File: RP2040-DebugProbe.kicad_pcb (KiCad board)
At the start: 2 copper layers, 55.9 x 25.4 mm, 60 parts, among them J1 CONN_MCU_JTAG, J10 CONN_USB, J2 CONN_MCU_UART, J3 CONN_DBG_COMB, J4 CONN_3V3_JUMPER, J7 CONN_DBG_JTAG, SW1 BOOTSEL, U1 W25Q128JVS, U2 RP2040, U3 74AUP1T17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

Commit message: Moved stuff around
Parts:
- moved D1 3.81 mm to (164.5, 104.1)
- moved D4 3.81 mm to (164.5, 99.0)
- moved D6 3.81 mm to (164.5, 111.7)
- moved D7 3.81 mm to (164.5, 116.8)
- moved J3 3.81 mm to (169.5, 99.1)
- moved J4 3.81 mm to (175.3, 99.0)
- moved J7 3.81 mm to (175.9, 118.1)
- moved R1 3.81 mm to (164.5, 105.4)
- moved R13 3.81 mm to (164.5, 115.6)
- moved R14 3.81 mm to (164.5, 102.9)
- moved R15 3.81 mm to (164.5, 100.3)
- moved R16 3.81 mm to (164.5, 114.3)
- moved R17 3.81 mm to (164.5, 113.0)
- moved R2 3.81 mm to (164.5, 97.8)
- moved R4 3.81 mm to (164.5, 110.5)
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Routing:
- net +3V3: track 44.1 -> 54.8 mm, vias 4 -> 7
- net XIN: track 0.00 -> 10.4 mm
- net MCU_RESET: track 0.00 -> 6.81 mm
- net XOUT: track 0.00 -> 5.68 mm
- net +1V1: track 10.3 -> 15.4 mm
- net SHIELD: track 7.66 -> 11.8 mm
- net VUSB: track 52.8 -> 49.0 mm
- net GND: track 2.28 -> 4.25 mm, vias 19 -> 21
- net USB_DN: track 21.5 -> 19.6 mm
- net USB_DP: track 21.6 -> 19.7 mm
- net QSPI_SD3: track 15.1 -> 13.2 mm
- net QSPI_SD1: track 12.3 -> 14.2 mm
- net QSPI_SD2: track 11.5 -> 13.4 mm
- net QSPI_SCLK: track 12.9 -> 11.1 mm
- net QSPI_SS: track 25.1 -> 26.9 mm
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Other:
- board size 55.9 x 25.4 mm -> 50.8 x 25.4 mm
- board text added: "G"
- board text added: "R"
- board text added: "T"

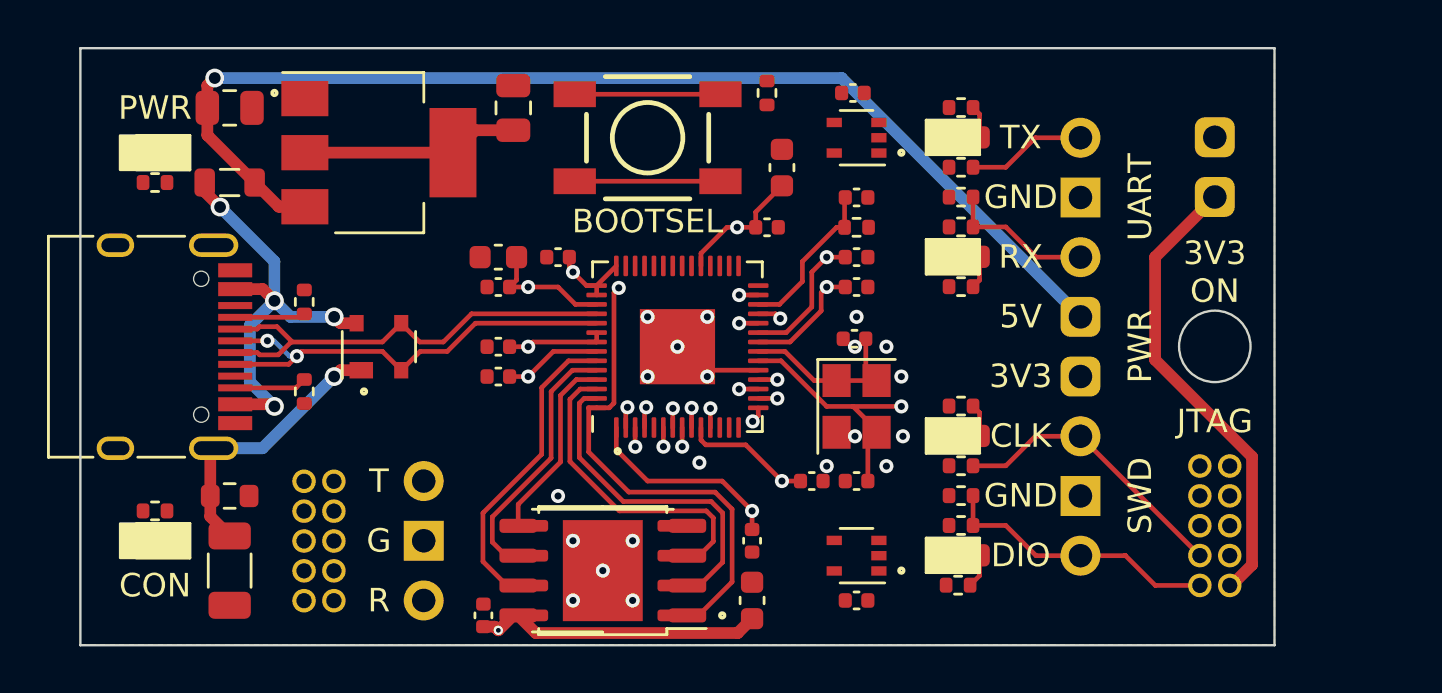
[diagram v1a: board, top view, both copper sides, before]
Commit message: Made the board 4 layer. Made a basic routing.
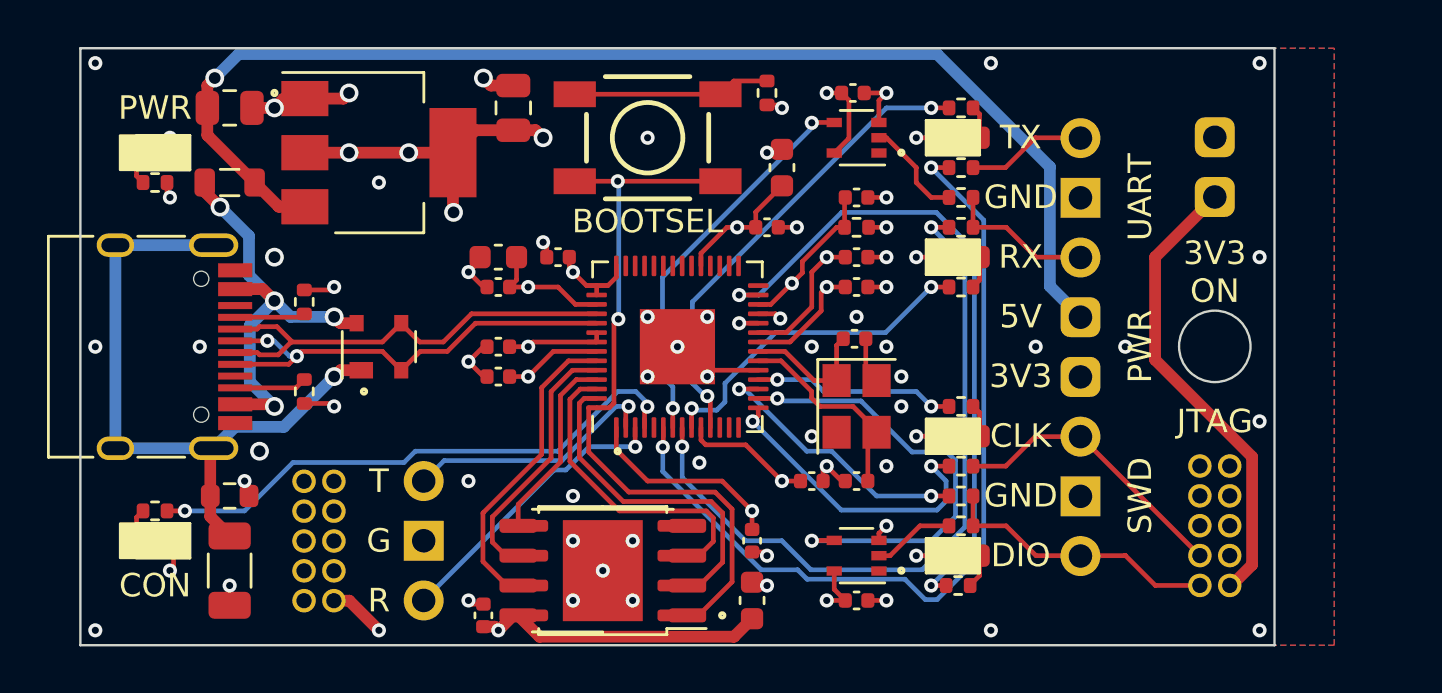
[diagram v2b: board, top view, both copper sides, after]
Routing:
- net MCU_CLK: track 0.81 -> 37.2 mm
- net UART_TX: track 0.82 -> 36.7 mm, vias 1 -> 2
- net GND: track 4.25 -> 37.7 mm, vias 21 -> 65
- net UART_RX: track 0.82 -> 30.6 mm, vias 1 -> 2
- net MCU_DIO: track 1.02 -> 30.7 mm
- net LED_RUN: track 0.81 -> 28.6 mm, vias 1 -> 2
- net MCU_RESET: track 6.81 -> 30.9 mm, vias 0 -> 1
- net LED_ACT: track 0.89 -> 23.8 mm, vias 1 -> 2
- net LED_TX: track 0.82 -> 20.1 mm, vias 1 -> 2
- net DBG_DIO_BUF: track 0.81 -> 19.4 mm, vias 1 -> 2
- net +1V1: track 15.4 -> 32.7 mm
- net SHIELD: track 11.8 -> 28.8 mm
- net UART_RX_BUF: track 0.82 -> 16.7 mm, vias 1 -> 2
- net +3V3: track 54.8 -> 68.9 mm, vias 7 -> 16
- net LED_RX: track 0.84 -> 14.4 mm, vias 1 -> 2
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- added copper zone on In2.Cu, net +3V3
- added copper zone on In1.Cu, net GND
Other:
- copper layers 2 -> 4
- board text added: "${TITLE} ${COMPANY} ${COMMENT2}"
